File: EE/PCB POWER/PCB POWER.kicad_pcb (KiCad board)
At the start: 2 copper layers, 84 x 84 mm, 51 parts, among them IC1 DRV8220DRLR, J1 1752104, J10 BM02B-GHS-TBT_LF__SN_, J11 BM02B-GHS-TBT_LF__SN_, J12 BM02B-GHS-TBT_LF__SN_, J13 BM02B-GHS-TBT_LF__SN_, J2 T1M-02-F-SV-L, J3 T1M-02-F-SV-L, J4 T1M-02-F-SV-L, J6 T1M-02-F-SV-L, J7 T1M-02-F-SV-L, J8 T1M-05-F-SV-L-P, J9 BM05B-GHS-TBT_LF__SN_, Q1 IPD30N08S2L21ATMA1, Q2 IPD30N08S2L21ATMA1, U1 MIC4427YM-TR, U2 742792510, U3 RPM5.0-6.0, U4 7427932

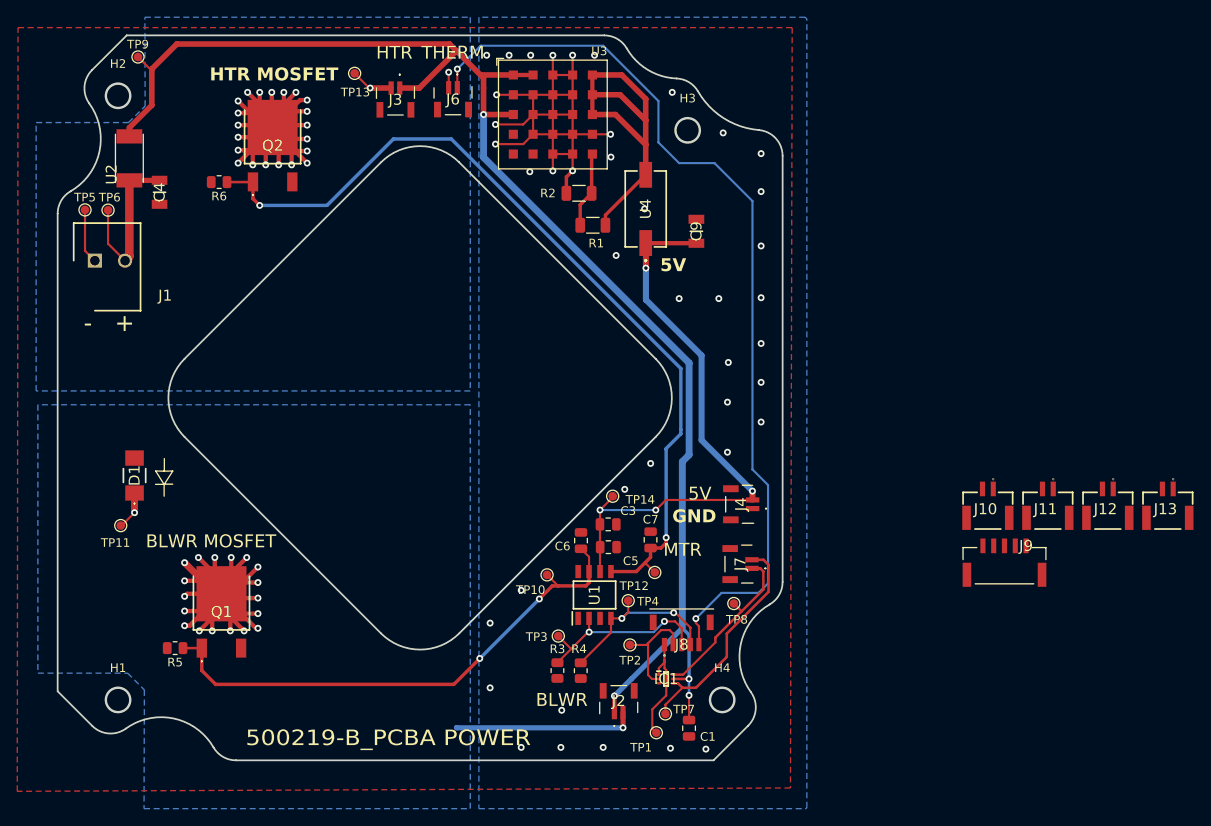
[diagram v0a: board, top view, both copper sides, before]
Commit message: Connectors and LED
moved to 2 mm pitch JST connectors
added LED to indicate board is powered
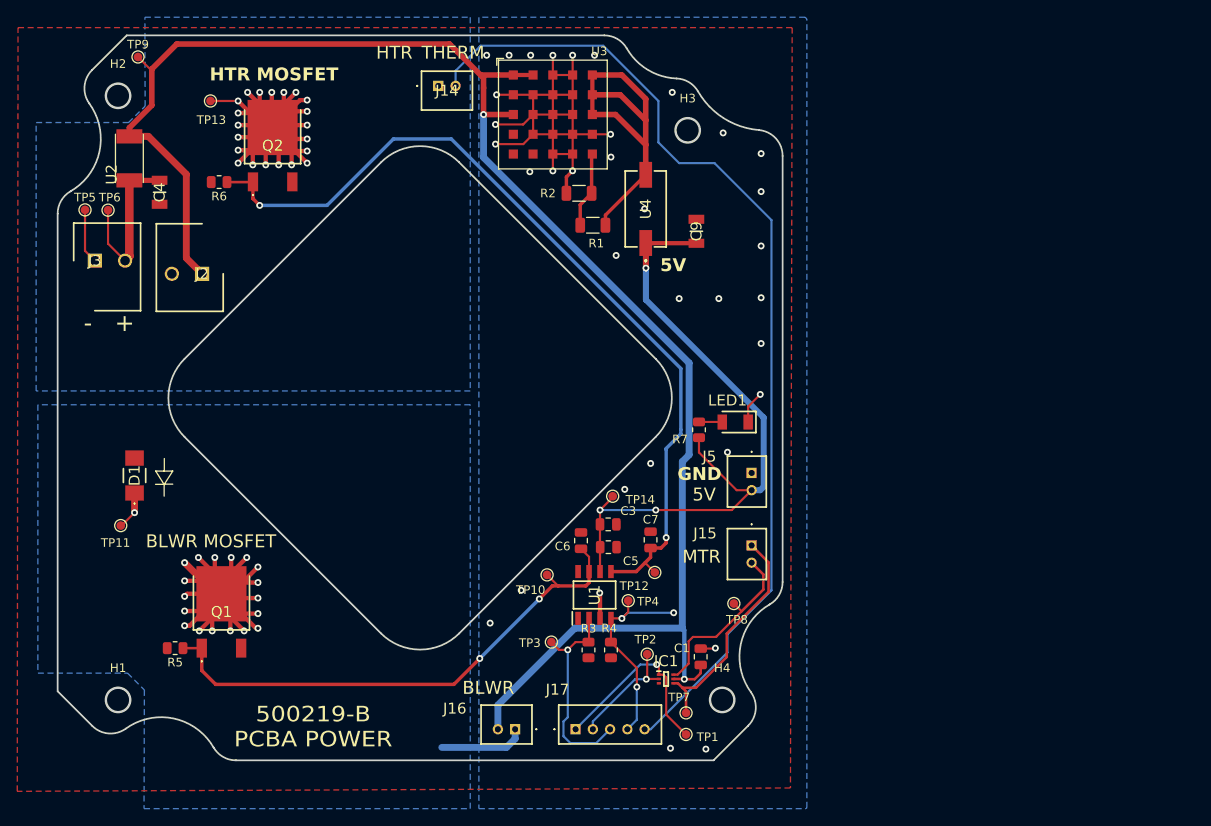
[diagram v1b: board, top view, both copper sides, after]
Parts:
- removed J1: 1752104, DaisyBio_Mira:SHDR2W90P0X350_1X2_760X1000X1255P
- removed J10, J11, J12, J13: BM02B-GHS-TBT_LF__SN_, DaisyBio_Mira:BM02B-GHS-TBT_1
- removed J4, J6, J7: T1M-02-F-SV-L, DaisyBio_Mira:T1M02FSVL
- removed J8: T1M-05-F-SV-L-P, DaisyBio_Mira:T1M-05-X-SV-L-Y
- removed J9: BM05B-GHS-TBT_LF__SN_, DaisyBio_Mira:BM05B-GHS-TBT
- added J14: B2B-PH-K-S, B2B-PH-K-S:B2BPHKS, F.Cu at (102.1, 63.9)
- added J15: B2B-PH-K-S, B2B-PH-K-S:B2BPHKS, F.Cu at (138.4, 117.1)
- added J16: B2B-PH-K-S, B2B-PH-K-S:B2BPHKS, F.Cu at (111.0, 138.4)
- added J17: B5B-PH-K-S, B5B-PH-K-S:B5BPHKS, F.Cu at (118.0, 138.4)
- added J5: B2B-PH-K-S, B2B-PH-K-S:B2BPHKS, F.Cu at (138.4, 108.7)
- added LED1: 150120VS75000, 150120VS75000:LEDC3216X78N, F.Cu at (136.5, 102.8)
- added R7: 280, Resistor_SMD:R_0805_2012Metric, F.Cu at (132.3, 103.7)
- J2, J3: value T1M-02-F-SV-L -> 1752104; footprint DaisyBio_Mira:T1M02FSVL -> 1752104:SHDR2W90P0X350_1X2_760X1000X1255P
- moved J2 69.0 mm to (74.7, 85.6), turned to 180 degrees
- moved J3 39.4 mm to (62.3, 84.1), turned to 0 degrees
- moved TP13 17.0 mm to (75.7, 65.6)
- moved C1 8.39 mm to (132.5, 130.0), turned to -90 degrees
- moved R3 4.32 mm to (119.5, 129.2)
- moved R4 4.24 mm to (122.1, 129.2)
- moved TP1 3.45 mm to (130.8, 139.0)
- moved TP7 2.39 mm to (130.8, 136.5)
- moved TP2 2.27 mm to (126.3, 129.7)
- moved TP3 1.06 mm to (115.2, 128.3)
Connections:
- J2 pad 2: Net-(D1-Pad1) -> Net-(J2-Pad2)
- J3 pad 1: Net-(IC1-VM) -> GND
- J3 pad 2: Net-(J3-Pad2) -> Net-(C4-Pad2)
- Q2 pad 2: Net-(J3-Pad2) -> Net-(J2-Pad2)
- TP13 pad 1: Net-(J3-Pad2) -> Net-(J2-Pad2)
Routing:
- net Net-(J3-Pad2): track 108.3 -> 0.00 mm, vias 22 -> 0
- net Net-(J2-Pad2): track 0.00 -> 106.5 mm, vias 0 -> 21
- net Net-(IC1-VM): track 170.0 -> 194.8 mm, vias 4 -> 2
- net Net-(D1-Pad1): track 121.2 -> 110.2 mm, vias 20 -> 19
- net Net-(U1-VS): track 68.3 -> 78.8 mm, vias 4 -> 3
- net THERM: track 106.0 -> 116.2 mm, vias 2 -> 0
- net MTR_PID1: track 12.9 -> 22.3 mm, vias 0 -> 1
- net GND: track 79.1 -> 85.8 mm, vias 42 -> 35
- net HTR_PID: track 21.1 -> 24.9 mm, vias 2 -> 3
- net Net-(LED1-A): track 0.00 -> 2.71 mm
- net BLWR_PID: track 22.3 -> 24.4 mm, vias 2 -> 1
- net MTR_1: track 19.7 -> 21.0 mm
- net MTR_PID2: track 12.3 -> 13.5 mm, vias 0 -> 1
- added copper zone on B.Cu, net Net-(J2-Pad2)
- removed copper zone on B.Cu, net Net-(J3-Pad2)
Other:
- board text added: "500219-B PCBA POWER"
- board text removed: "500219-B_PCBA POWER"

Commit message: Small fixes
Small fixes
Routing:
- net GND: vias 35 -> 37
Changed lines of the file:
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@@
 		)
 		(fp_text user "${REFERENCE}"
-			(at -4 0.55 0)
+			(at 2.1 4.6 0)
 			(layer "F.Fab")
 			(effects
@@
 		(tags "test point SMD pad")
 		(property "Reference" "TP7"
-			(at -0.8 -1.8 0)
+			(at -0.4 -1.6 0)
 			(layer "F.SilkS")
 			(effects
@@
 		)
 		(fp_text user "${REFERENCE}"
-			(at -0.8 -1.8 0)
+			(at -0.4 -1.6 0)
 			(layer "F.Fab")
 			(effects
@@
 		(tags "Integrated Circuit")
 		(property "Reference" "IC1"
-			(at 0 -2.07 0)
+			(at 0.21 -2.17 0)
 			(layer "F.SilkS")
 			(effects
@@
 		)
 		(fp_text user "${REFERENCE}"
-			(at 0 -2.07 0)
+			(at 0.21 -2.17 0)
 			(layer "F.Fab")
 			(effects
@@
 		(tags "test point SMD pad")
 		(property "Reference" "TP14"
-			(at 3.2 0.4 0)
+			(at 2.7 -0.9 0)
 			(layer "F.SilkS")
 			(effects
@@
 		)
 		(fp_text user "${REFERENCE}"
-			(at 3.2 0.4 0)
+			(at 2.7 -0.9 0)
 			(layer "F.Fab")
 			(effects
@@
 		(tags "Ferrite Bead")
 		(property "Reference" "U4"
-			(at 0 0 90)
+			(at 3.01 4.67 180)
 			(layer "F.SilkS")
 			(effects
@@
 		)
 		(fp_text user "${REFERENCE}"
-			(at 0 0 90)
+			(at 3.01 4.67 180)
 			(layer "F.Fab")
 			(effects
@@
 		(tags "Connector")
 		(property "Reference" "J14"
-			(at -1 -0.55 0)
+			(at -1 -4.55 0)
 			(layer "F.SilkS")
 			(effects
@@
 		)
 		(fp_text user "${REFERENCE}"
-			(at -1 -0.55 0)
+			(at -1 -4.55 0)
 			(layer "F.Fab")
 			(effects
@@
 		(tags "Connector")
 		(property "Reference" "J5"
-			(at 1.9 -4.9 180)
+			(at 2.2 -5 180)
 			(layer "F.SilkS")
 			(effects
@@
 		)
 		(fp_text user "${REFERENCE}"
-			(at 1.9 -4.9 180)
+			(at 2.2 -5 180)
 			(layer "F.Fab")
 			(effects
@@
 		(tags "resistor")
 		(property "Reference" "R3"
-			(at -2.4875 0 180)
+			(at 2.6875 0 180)
 			(layer "F.SilkS")
 			(effects
@@
 		(tags "capacitor")
 		(property "Reference" "C1"
-			(at -0.99 2.18 0)
+			(at -2.4 0.2 0)
 			(layer "F.SilkS")
 			(effects
@@
 		(tags "test point SMD pad")
 		(property "Reference" "TP12"
-			(at -2.38 1.57 0)
+			(at 2.82 1.47 0)
 			(layer "F.SilkS")
 			(effects
@@
 		)
 		(fp_text user "${REFERENCE}"
-			(at 2.64 -1.2 0)
+			(at 2.82 1.47 0)
 			(layer "F.Fab")
 			(effects
@@
 		(tags "resistor")
 		(property "Reference" "R4"
-			(at -2.5125 0.2 0)
+			(at 2.6875 0 0)
 			(layer "F.SilkS")
 			(effects
@@
 	)
 	(image
-		(at 135.536748 92.322893)
+		(at 134.8 91.100001)
 		(layer "F.SilkS")
-		(scale 0.237245)
+		(scale 0.261638)
 		(data "iVBORw0KGgoAAAANSUhEUgAAAF8AAABkCAYAAADg8eybAAAABHNCSVQICAgIfAhkiAAAAAlwSFlz"
 			"AAAHpgAAB6YBHZXXMwAAABl0RVh0U29mdHdhcmUAd3d3Lmlua3NjYXBlLm9yZ5vuPBoAABOzSURB"
@@
 	)
 	(via
+		(at 120.3 133.5)
+		(size 0.8)
+		(drill 0.4)
+		(layers "F.Cu" "B.Cu")
+		(free yes)
+		(net 2)
+	)
+	(via
 		(at 115.37 60.31)
 		(size 0.8)
@@
 		(size 0.8)
 		(drill 0.4)
+		(layers "F.Cu" "B.Cu")
+		(free yes)
+		(net 2)
+	)
+	(via
+		(at 129.1 128.3)
+		(size 0.8)
+		(drill 0.4)

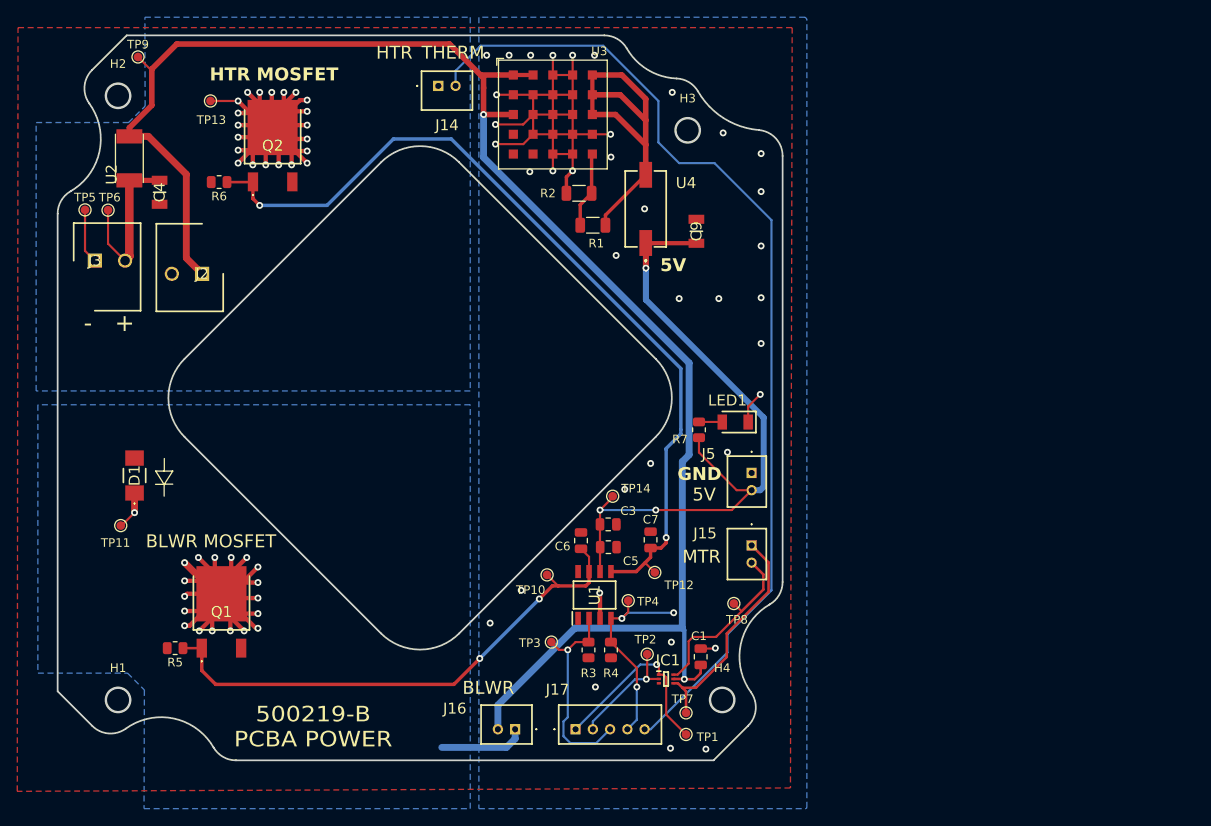
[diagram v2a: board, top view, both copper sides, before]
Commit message: Minor adjustments
moved screen printed text
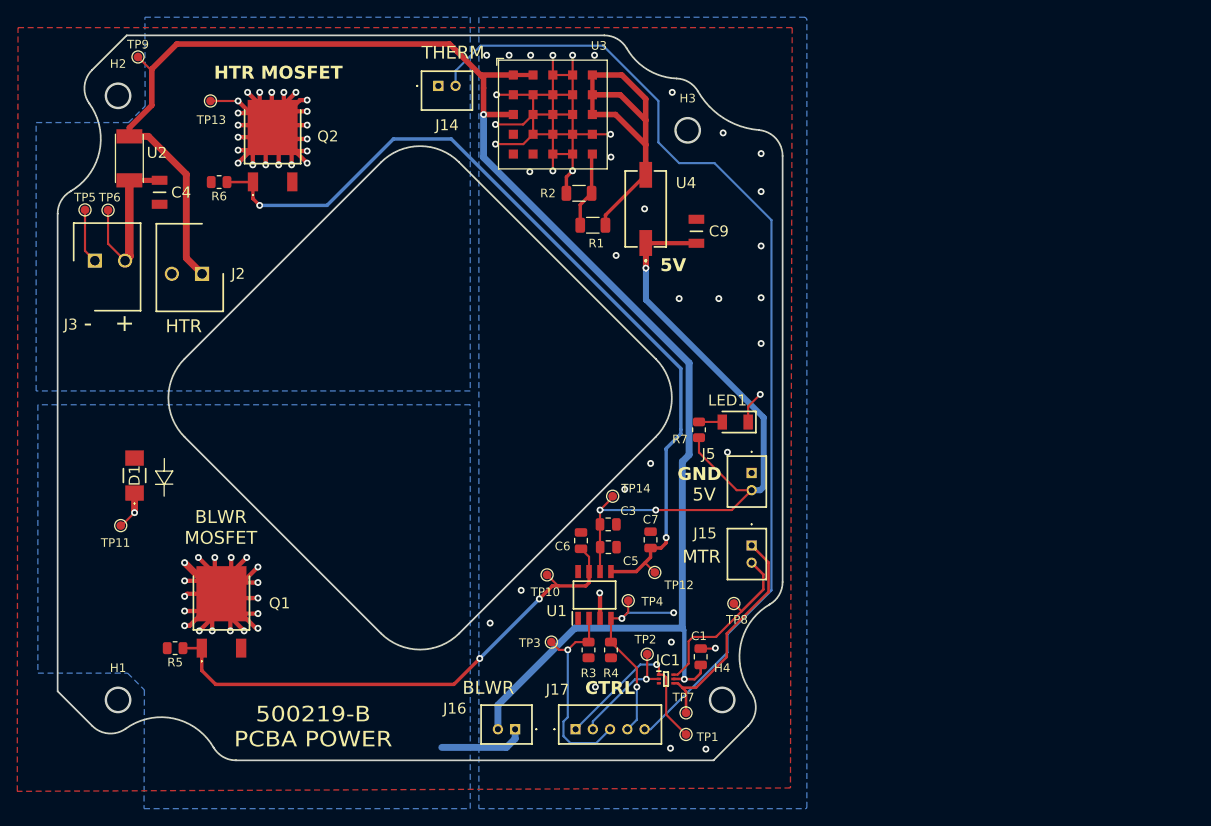
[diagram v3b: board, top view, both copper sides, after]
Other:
- board text added: "CTRL"
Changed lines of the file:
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@@
 			)
 		)
+		(model "${KICAD9_3DMODEL_DIR}/Connector_JST.3dshapes/JST_PH_B5B-PH-K_1x05_P2.00mm_Vertical.step"
+			(offset
+				(xyz -8 -0 0)
+			)
+			(scale
+				(xyz 1 1 1)
+			)
+			(rotate
+				(xyz -0 -0 -0)
+			)
+		)
 	)
 	(footprint "Resistor_SMD:R_1206_3216Metric"
@@
 		(tags "test point SMD pad")
 		(property "Reference" "TP7"
-			(at -0.4 -1.6 0)
+			(at -0.3 -1.8 0)
 			(layer "F.SilkS")
 			(effects
@@
 		)
 		(fp_text user "${REFERENCE}"
-			(at -0.4 -1.6 0)
+			(at -0.3 -1.8 0)
 			(layer "F.Fab")
 			(effects
@@
 		(tags "Integrated Circuit")
 		(property "Reference" "U1"
-			(at 0 0 90)
+			(at -1.86 -4.4 180)
 			(layer "F.SilkS")
 			(effects
@@
 		)
 		(fp_text user "${REFERENCE}"
-			(at 0 0 90)
+			(at -1.86 -4.4 180)
 			(layer "F.Fab")
 			(effects
@@
 		(tags "Capacitor")
 		(property "Reference" "C4"
-			(at 0 0 90)
+			(at -0.02 2.5 180)
 			(layer "F.SilkS")
 			(effects
@@
 		)
 		(fp_text user "${REFERENCE}"
-			(at 0 0 90)
+			(at 0 2.5 180)
 			(layer "F.Fab")
 			(effects
@@
 			)
 		)
+		(model "${KICAD9_3DMODEL_DIR}/Connector_JST.3dshapes/JST_PH_B2B-PH-K_1x02_P2.00mm_Vertical.step"
+			(offset
+				(xyz 0 0.25 0)
+			)
+			(scale
+				(xyz 1 1 1)
+			)
+			(rotate
+				(xyz -0 -0 -180)
+			)
+		)
 	)
 	(footprint "Resistor_SMD:R_0805_2012Metric"
@@
 		(tags "MOSFET (N-Channel)")
 		(property "Reference" "Q2"
-			(at 0 1.02 0)
+			(at 6.4 -0.05 0)
 			(layer "F.SilkS")
 			(effects
@@
 		(tags "MOSFET (N-Channel)")
 		(property "Reference" "Q1"
-			(at 0 1.02 0)
+			(at 6.73 0.02 0)
 			(layer "F.SilkS")
 			(effects
@@
 		)
 		(fp_text user "${REFERENCE}"
-			(at -2.27 1.41 180)
+			(at -2 -0.6 180)
 			(layer "F.Fab")
 			(effects
@@
 			)
 		)
+		(model "${KICAD9_3DMODEL_DIR}/Connector_JST.3dshapes/JST_PH_B2B-PH-K_1x02_P2.00mm_Vertical.step"
+			(offset
+				(xyz 0 0 0)
+			)
+			(scale
+				(xyz 1 1 1)
+			)
+			(rotate
+				(xyz -0 -0 -180)
+			)
+		)
 	)
 	(footprint "B2B-PH-K-S:B2BPHKS"
@@
 			)
 		)
+		(model "${KICAD9_3DMODEL_DIR}/Connector_JST.3dshapes/JST_PH_B2B-PH-K_1x02_P2.00mm_Vertical.step"
+			(offset
+				(xyz 0 0 0)
+			)
+			(scale
+				(xyz 1 1 1)
+			)
+			(rotate
+				(xyz -0 -0 -180)
+			)
+		)
 	)
 	(footprint "TestPoint:TestPoint_Pad_D1.0mm"
@@
 		(tags "test point SMD pad")
 		(property "Reference" "TP4"
-			(at 2.3 0.1 0)
+			(at 2.8 0.1 0)
 			(layer "F.SilkS")
 			(effects
@@
 		)
 		(fp_text user "${REFERENCE}"
-			(at 2.3 0.1 0)
+			(at 2.8 0.1 0)
 			(layer "F.Fab")
 			(effects
@@
 		(tags "dc-dc recom buck lga-25 pitch 2.29mm")
 		(property "Reference" "U3"
-			(at 5.38 -7.34 0)
+			(at 5.33 -7.97 0)
 			(layer "F.SilkS")
 			(effects
@@
 		)
 		(fp_text user "${REFERENCE}"
-			(at 0 0 0)
+			(at 5.33 -7.97 0)
 			(layer "F.Fab")
 			(effects
@@
 		(tags "Inductor")
 		(property "Reference" "U2"
-			(at -1.8575 -2.06 90)
+			(at 0.65 3.2 180)
 			(layer "F.SilkS")
 			(effects
@@
 		)
 		(fp_text user "${REFERENCE}"
-			(at -1.8575 -2.06 90)
+			(at 0.65 3.2 180)
 			(layer "F.Fab")
 			(effects
@@
 		(tags "test point SMD pad")
 		(property "Reference" "TP10"
-			(at -1.9 1.75 0)
+			(at -0.2 1.99 0)
 			(layer "F.SilkS")
 			(effects
@@
 		)
 		(fp_text user "${REFERENCE}"
-			(at -1.9 1.75 0)
+			(at -0.2 1.99 0)
 			(layer "F.Fab")
 			(effects
@@
 		(tags "Capacitor")
 		(property "Reference" "C9"
-			(at 0 0 270)
+			(at 0 -2.6 0)
 			(layer "F.SilkS")
 			(effects
@@
 		)
 		(fp_text user "${REFERENCE}"
-			(at 0 0 270)
+			(at 0 -2.6 0)
 			(layer "F.Fab")
 			(effects
@@
 			)
 		)
+		(model "${KICAD9_3DMODEL_DIR}/Connector_JST.3dshapes/JST_PH_B2B-PH-K_1x02_P2.00mm_Vertical.step"
+			(offset
+				(xyz 0 0 0)
+			)
+			(scale
+				(xyz 1 1 1)
+			)
+			(rotate
+				(xyz -0 -0 -180)
+			)
+		)
 	)
 	(footprint "TestPoint:TestPoint_Pad_D1.0mm"
@@
 		(tags "Connector")
 		(property "Reference" "J2"
-			(at 0 0 0)
+			(at -4.175 0 0)
 			(layer "F.SilkS")
 			(effects
@@
 		)
 		(fp_text user "${REFERENCE}"
-			(at 0 0 0)
+			(at -4.175 0 0)
 			(layer "F.Fab")
 			(effects
@@
 		(tags "Connector")
 		(property "Reference" "J3"
-			(at 0 0 0)
+			(at -2.8 7.4 0)
 			(layer "F.SilkS")
 			(effects
@@
 		)
 		(fp_text user "${REFERENCE}"
-			(at 0 0 0)
+			(at -2.8 7.4 0)
 			(layer "F.Fab")
 			(effects
@@
 		)
 	)
-	(gr_text "BLWR MOSFET"
-		(at 68.2 117.5 0)
+	(gr_text "BLWR\nMOSFET"
+		(at 76.9 117.1 0)
 		(layer "F.SilkS")
 		(effects
@@
 				(thickness 0.3)
 			)
-			(justify left bottom)
+			(justify bottom)
 		)
 	)
@@
 		)
 	)
+	(gr_text "CTRL"
+		(at 119.1 134.5 0)
+		(layer "F.SilkS")
+		(effects
+			(font
+				(size 1.5 1.5)
+				(thickness 0.3)
+				(bold yes)
+			)
+			(justify left bottom)
+		)
+	)
 	(gr_text "-"
 		(at 61 92.5 0)
@@
 	)
 	(gr_text "HTR MOSFET"
-		(at 75.6 63.4 0)
+		(at 76.1 63.2 0)
 		(layer "F.SilkS")
 		(effects
@@
 	)
 	(gr_text "HTR"
-		(at 97 60 0)
+		(at 72.6 91.7 0)
 		(layer "F.SilkS")
 		(effects

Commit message: Widened traces
Widened traces with higher current draw
Fixed some minor errors
Added change note calling out added LED
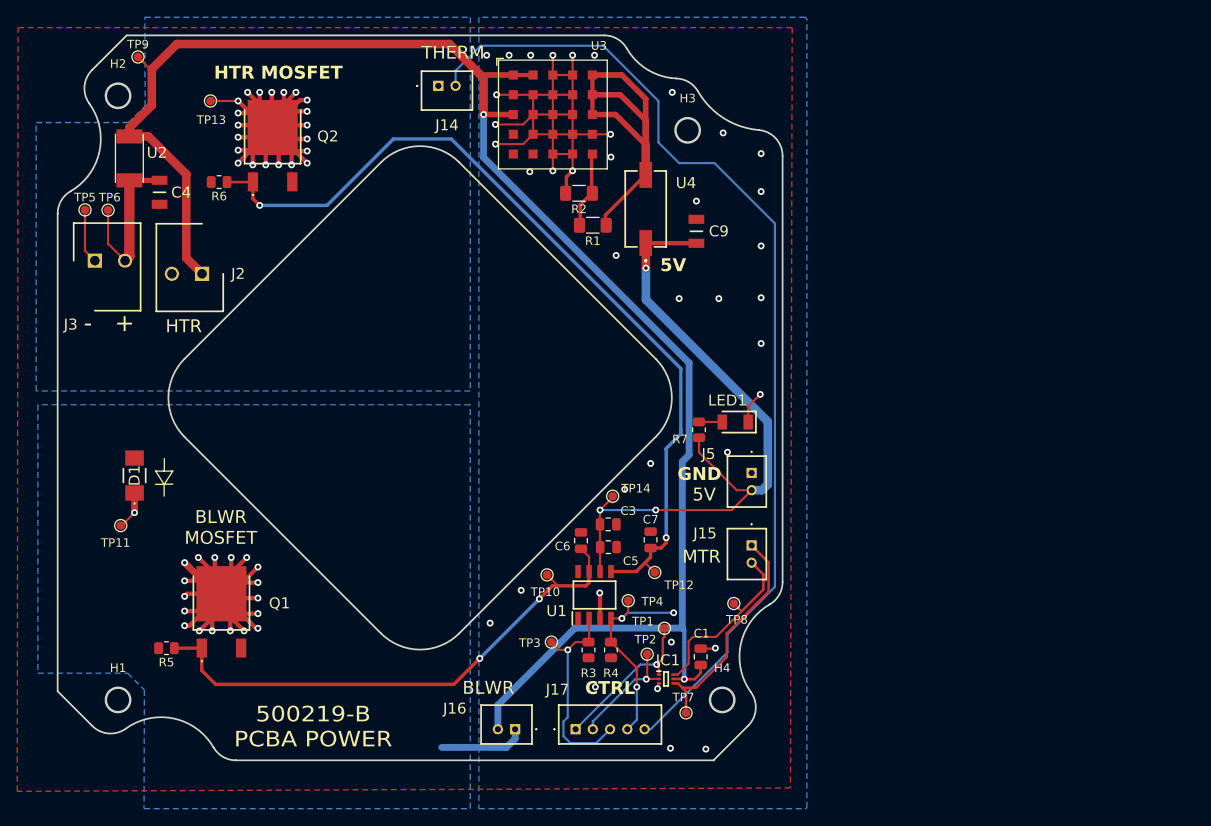
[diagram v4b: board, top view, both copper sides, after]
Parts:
- R1, R2: footprint Resistor_SMD:R_1206_3216Metric -> Resistor_SMD:R_1206_3216Metric_Pad1.30x1.75mm_HandSolder
- moved TP1 12.6 mm to (128.3, 126.7)
- moved R5 1.00 mm to (70.6, 129.0)
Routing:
- net MTR_PID1: track 22.3 -> 18.4 mm
- net Net-(U1-OUTA): track 61.3 -> 62.3 mm
- net GND: track 85.8 -> 86.5 mm, vias 37 -> 38
- net Net-(U1-VS): track 78.8 -> 79.3 mm
